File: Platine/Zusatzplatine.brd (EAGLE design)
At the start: 72.1 x 52.1 mm, 29 parts

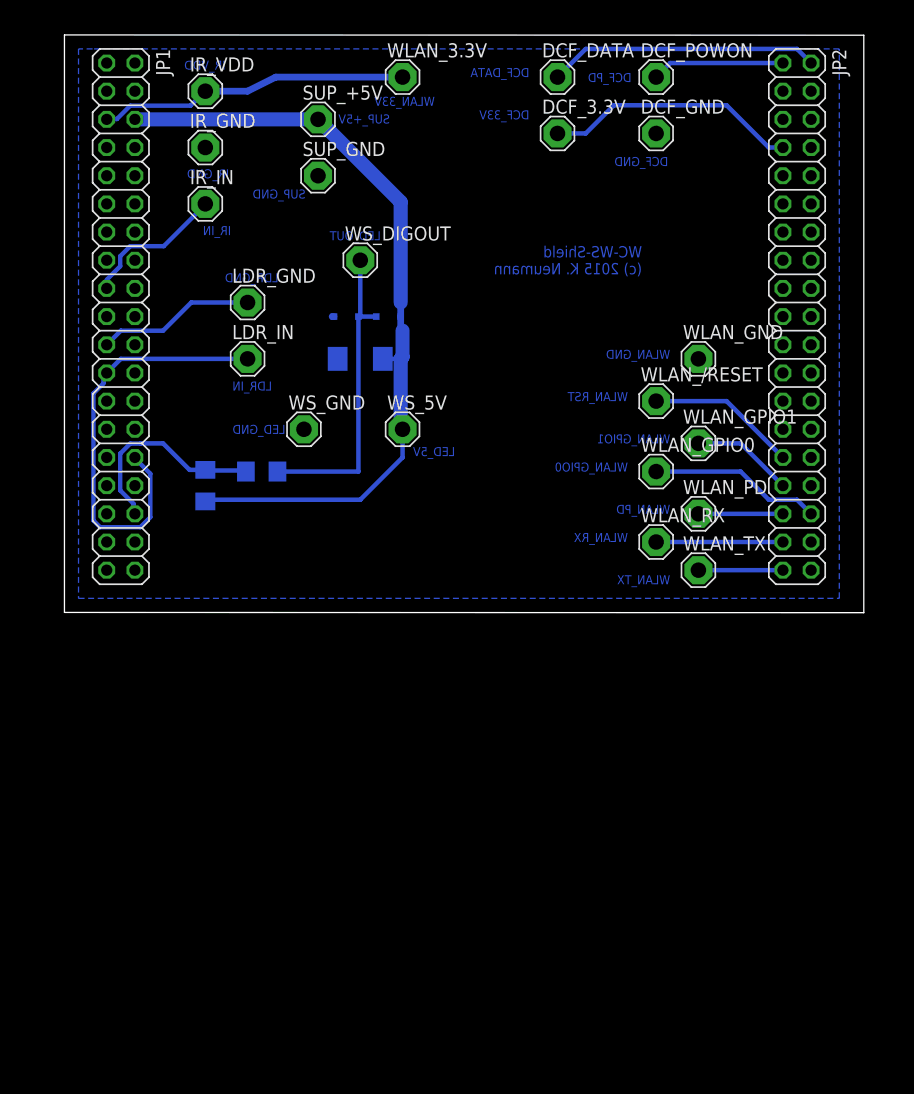
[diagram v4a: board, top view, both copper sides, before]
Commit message: - Platine auf Arduino Connectors umgestellt
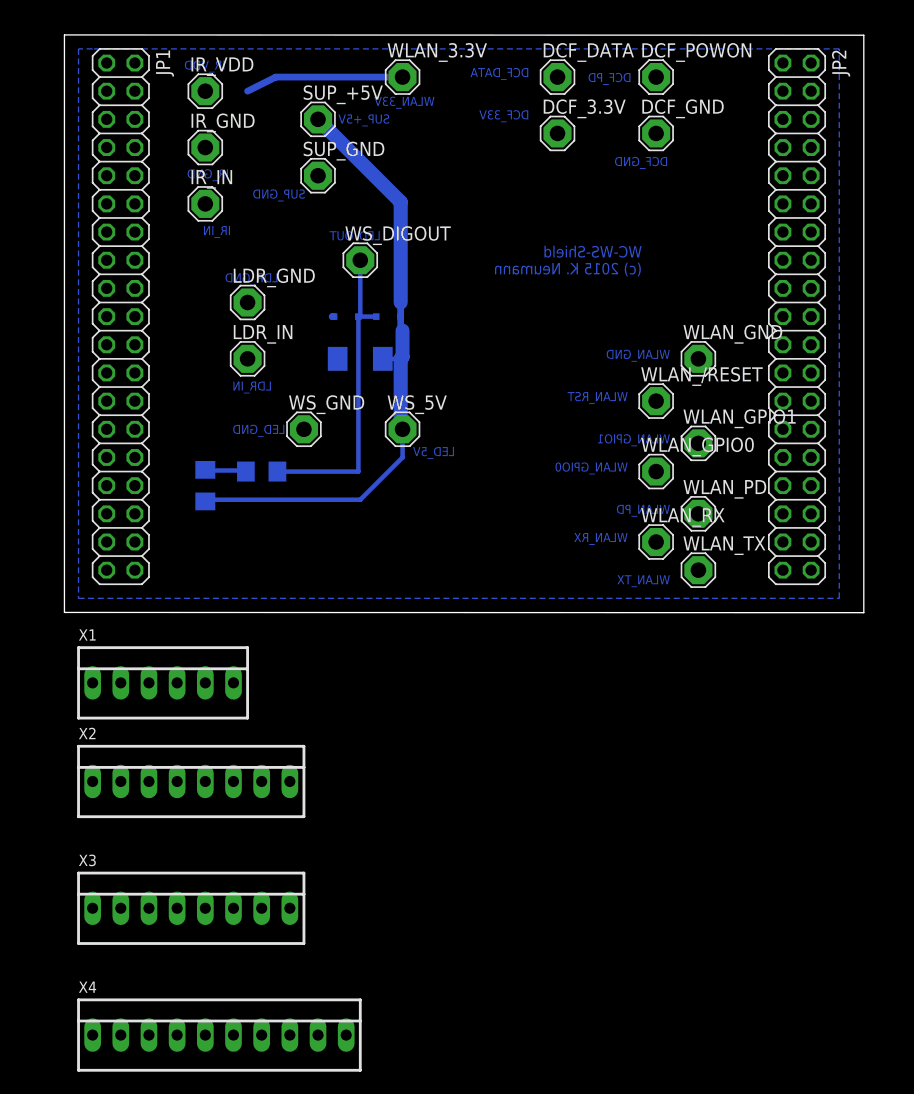
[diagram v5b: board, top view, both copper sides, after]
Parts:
- added X1: (no value), con-molex:22-23-2061
- added X2, X3: 22-23-2081, con-molex:22-23-2081
- added X4: 22-23-2101, con-molex:22-23-2101
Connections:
- removed net N$12: JP2.33, WLAN_PD.MP
- removed net N$13: JP2.35, WLAN_RX.MP
- removed net N$14: JP2.37, WLAN_TX.MP
- removed net N$15: JP2.34, WLAN_GPIO0.MP
- removed net N$18: DCF_3.3V.MP, JP2.7
- removed net N$19: DCF_POWON.MP, JP2.1
- removed net N$20: DCF_DATA.MP, JP2.2
- new net AVDD: X4.3
- new net N$10: DCF_POWON.MP, X4.1
- new net N$5: WLAN_PD.MP, X3.6
- new net N$7: WLAN_/RESET.MP, X3.4
- new net N$9: WLAN_GPIO0.MP, X3.3
- net +3.3V: now also X2.5; no longer JP1.5
- net +5V: now also X2.4; no longer JP1.6
- net GND: now also LDR_GND.MP, X2.2, X2.3; no longer JP1.20, JP1.22, JP1.8, JP2.20, JP2.9, WLAN_GND.MP
- net LED-OUT: now also X1.3; no longer JP1.34
- net N$1: now also WLAN_TX.MP, X3.8; no longer JP2.29, WLAN_/RESET.MP
- net N$11: now also DCF_DATA.MP, X4.2; no longer JP2.31, WLAN_GPIO1.MP
- net N$2: now also X1.6; no longer JP1.17
- net N$3: now also LDR_IN.MP, X1.4, X1.5; no longer JP1.21, LDR_GND.MP
- net N$4: now also WLAN_RX.MP, X3.7; no longer JP1.19
- net N$6: now also WLAN_GPIO1.MP, X3.5; no longer JP1.23, JP1.30, LDR_IN.MP
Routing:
- net N$6: track 38.9 -> 0.00 mm
- net N$20: track 24.4 -> 0.00 mm
- net N$18: track 23.0 -> 0.00 mm
- net +5V: track 71.5 -> 55.0 mm
- net N$15: track 15.5 -> 0.00 mm
- net LED-OUT: track 18.9 -> 3.69 mm
- net N$3: track 14.3 -> 0.00 mm
- net +3.3V: track 28.0 -> 14.3 mm
- net N$1: track 13.5 -> 0.00 mm
- net N$2: track 13.1 -> 0.00 mm
- net N$19: track 12.0 -> 0.00 mm
- net N$13: track 11.4 -> 0.00 mm
- net N$11: track 9.20 -> 0.00 mm
- net N$14: track 7.62 -> 0.00 mm
- net N$12: track 7.62 -> 0.00 mm

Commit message: - Platine überarbeitet
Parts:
- removed JP1, JP2: (no value), pinhead:2X19
- moved X4 88.9 mm to (63.5, 49.5), turned to 270 degrees
- moved X3 62.3 mm to (63.5, 24.1), turned to 270 degrees
- moved X2 45.7 mm to (15.2, 41.9), turned to 90 degrees
- moved IR_IN 20.9 mm to (21.6, 27.9)
- moved WLAN_3.3V 17.7 mm to (27.9, 43.2)
- moved X1 16.7 mm to (15.2, 21.6), turned to 90 degrees
- moved IR_VDD 16.1 mm to (21.6, 43.2)
- moved R2 15.3 mm to (31.8, 21.6), turned to 180 degrees
- moved WLAN_GND 12.7 mm to (48.3, 34.3)
- moved WLAN_PD 12.7 mm to (48.3, 20.3)
- moved WLAN_TX 12.7 mm to (48.3, 15.2)
- moved WS_GND 12.7 mm to (38.1, 27.9)
- moved LDR_IN 11.5 mm to (21.6, 22.9)
- moved WLAN_/RESET 9.67 mm to (48.3, 26.7)
- moved R1 9.25 mm to (30.5, 26.7), turned to 90 degrees
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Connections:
- net AVDD: now also DCF_3.3V.MP
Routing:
- net +5V: track 55.0 -> 23.1 mm
- net LED-OUT: track 3.69 -> 21.4 mm
- net N$11: track 0.00 -> 16.8 mm
- net N$7: track 0.00 -> 15.8 mm
- net AVDD: track 0.00 -> 15.8 mm
- net N$5: track 0.00 -> 15.2 mm
- net N$1: track 0.00 -> 15.2 mm
- net N$9: track 0.00 -> 12.5 mm
- net N$6: track 0.00 -> 12.0 mm
- net N$4: track 0.00 -> 11.4 mm
- net N$3: track 0.00 -> 8.89 mm
- net N$10: track 0.00 -> 6.88 mm
- net N$2: track 0.00 -> 6.35 mm
- net N$8: track 28.1 -> 21.8 mm
- net +3.3V: track 14.3 -> 12.7 mm
- added copper zone on layer 1, net +5V
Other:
- board size 72.1 x 52.1 mm -> 55.6 x 49.5 mm
- board text added: "IR_+3.3V"
- board text removed: "IR_VDD"

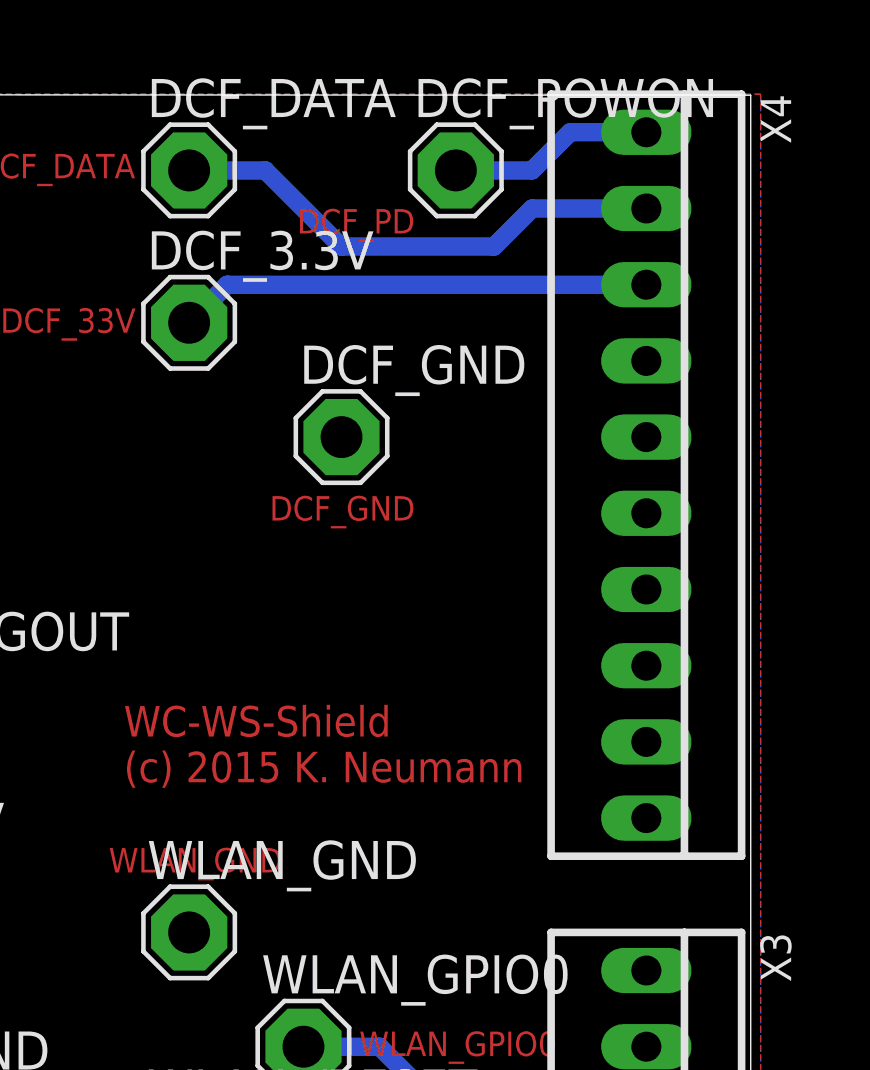
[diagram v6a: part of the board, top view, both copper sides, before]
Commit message: Corrected layout of top right pin row for arduino interfacing
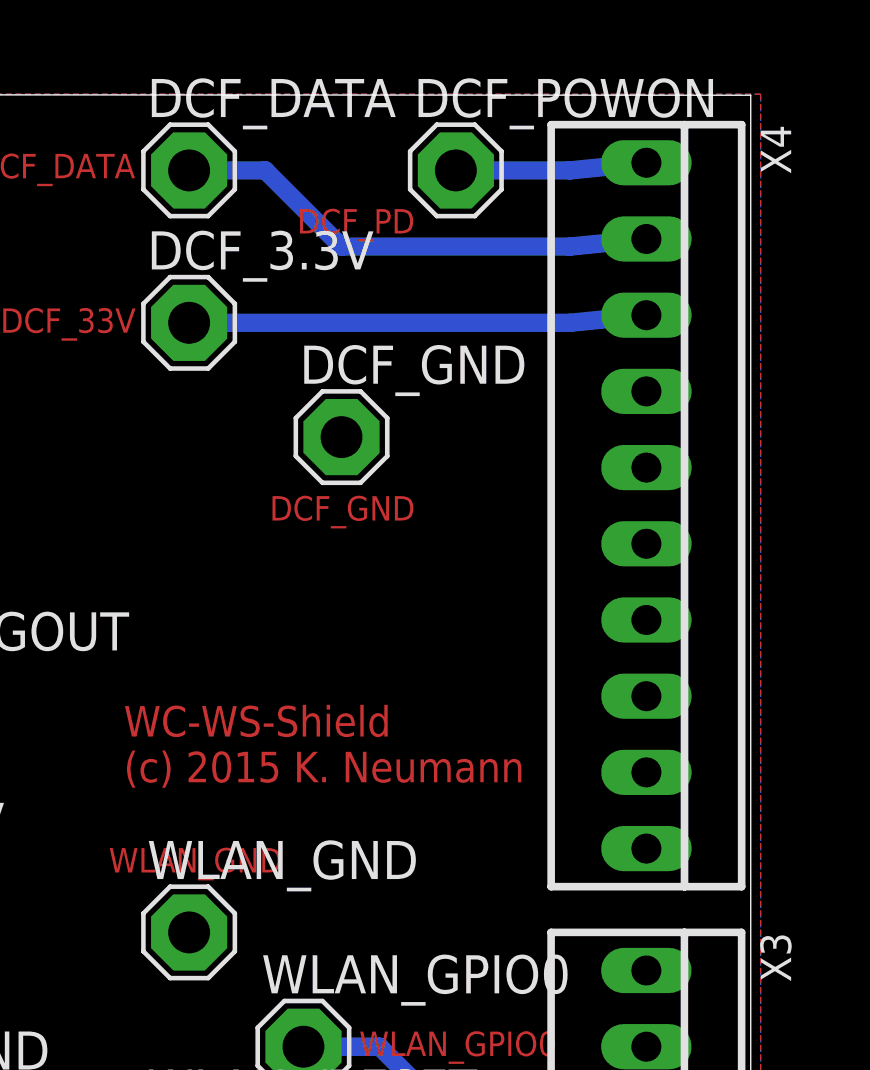
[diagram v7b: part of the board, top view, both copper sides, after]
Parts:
- moved X4 1.02 mm to (63.5, 48.5)
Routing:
- net N$11: track 16.8 -> 16.3 mm
- net N$10: track 6.88 -> 6.36 mm
- net AVDD: track 15.8 -> 15.3 mm
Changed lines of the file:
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@@
 <?xml version="1.0" encoding="utf-8"?>
 <!DOCTYPE eagle SYSTEM "eagle.dtd">
-<eagle version="7.4.0">
+<eagle version="7.2.0">
 <drawing>
 <settings>
@@
 <layer number="48" name="Document" color="7" fill="1" visible="yes" active="yes"/>
 <layer number="49" name="Reference" color="7" fill="1" visible="yes" active="yes"/>
+<layer number="50" name="dxf" color="7" fill="1" visible="no" active="yes"/>
 <layer number="51" name="tDocu" color="7" fill="1" visible="yes" active="yes"/>
 <layer number="52" name="bDocu" color="7" fill="1" visible="yes" active="yes"/>
+<layer number="53" name="tGND_GNDA" color="7" fill="9" visible="no" active="no"/>
+<layer number="54" name="bGND_GNDA" color="1" fill="9" visible="no" active="no"/>
+<layer number="56" name="wert" color="7" fill="1" visible="no" active="yes"/>
+<layer number="57" name="tCAD" color="7" fill="1" visible="no" active="no"/>
 <layer number="90" name="Modules" color="5" fill="1" visible="no" active="no"/>
 <layer number="91" name="Nets" color="2" fill="1" visible="no" active="no"/>
@@
 <layer number="98" name="Guide" color="6" fill="1" visible="no" active="no"/>
 <layer number="99" name="SpiceOrder" color="5" fill="1" visible="no" active="no"/>
+<layer number="100" name="Muster" color="7" fill="1" visible="no" active="no"/>
+<layer number="101" name="Patch_Top" color="12" fill="4" visible="no" active="yes"/>
+<layer number="102" name="Vscore" color="7" fill="1" visible="no" active="yes"/>
+<layer number="103" name="fp3" color="7" fill="1" visible="no" active="yes"/>
+<layer number="104" name="Name" color="7" fill="1" visible="no" active="yes"/>
+<layer number="105" name="Beschreib" color="9" fill="1" visible="no" active="yes"/>
+<layer number="106" name="BGA-Top" color="4" fill="1" visible="no" active="yes"/>
+<layer number="107" name="BD-Top" color="5" fill="1" visible="no" active="yes"/>
+<layer number="108" name="fp8" color="7" fill="1" visible="no" active="yes"/>
+<layer number="109" name="fp9" color="7" fill="1" visible="no" active="yes"/>
+<layer number="110" name="fp0" color="7" fill="1" visible="no" active="yes"/>
+<layer number="111" name="LPC17xx" color="7" fill="1" visible="no" active="yes"/>
+<layer number="112" name="tSilk" color="7" fill="1" visible="no" active="yes"/>
+<layer number="113" name="ReferenceLS" color="7" fill="1" visible="no" active="no"/>
+<layer number="116" name="Patch_BOT" color="9" fill="4" visible="no" active="yes"/>
+<layer number="118" name="Rect_Pads" color="7" fill="1" visible="no" active="no"/>
+<layer number="121" name="_tsilk" color="7" fill="1" visible="no" active="yes"/>
+<layer number="122" name="_bsilk" color="7" fill="1" visible="no" active="yes"/>
+<layer number="123" name="tTestmark" color="7" fill="1" visible="no" active="yes"/>
+<layer number="124" name="bTestmark" color="7" fill="1" visible="no" active="yes"/>
+<layer number="125" name="_tNames" color="7" fill="1" visible="no" active="yes"/>
+<layer number="126" name="_bNames" color="7" fill="1" visible="no" active="yes"/>
+<layer number="127" name="_tValues" color="7" fill="1" visible="no" active="yes"/>
+<layer number="128" name="_bValues" color="7" fill="1" visible="no" active="yes"/>
+<layer number="131" name="tAdjust" color="7" fill="1" visible="no" active="yes"/>
+<layer number="132" name="bAdjust" color="7" fill="1" visible="no" active="yes"/>
+<layer number="144" name="Drill_legend" color="7" fill="1" visible="no" active="yes"/>
+<layer number="150" name="Notes" color="7" fill="1" visible="no" active="yes"/>
+<layer number="151" name="HeatSink" color="7" fill="1" visible="no" active="yes"/>
+<layer number="152" name="_bDocu" color="7" fill="1" visible="no" active="yes"/>
+<layer number="153" name="FabDoc1" color="6" fill="1" visible="no" active="no"/>
+<layer number="154" name="FabDoc2" color="2" fill="1" visible="no" active="no"/>
+<layer number="155" name="FabDoc3" color="7" fill="15" visible="no" active="no"/>
+<layer number="199" name="Contour" color="7" fill="1" visible="no" active="yes"/>
+<layer number="200" name="200bmp" color="1" fill="10" visible="no" active="yes"/>
+<layer number="201" name="201bmp" color="2" fill="1" visible="no" active="no"/>
+<layer number="202" name="202bmp" color="3" fill="1" visible="no" active="no"/>
+<layer number="203" name="203bmp" color="4" fill="10" visible="no" active="yes"/>
+<layer number="204" name="204bmp" color="5" fill="10" visible="no" active="yes"/>
+<layer number="205" name="205bmp" color="6" fill="10" visible="no" active="yes"/>
+<layer number="206" name="206bmp" color="7" fill="10" visible="no" active="yes"/>
+<layer number="207" name="207bmp" color="8" fill="10" visible="no" active="yes"/>
+<layer number="208" name="208bmp" color="9" fill="10" visible="no" active="yes"/>
+<layer number="209" name="209bmp" color="7" fill="1" visible="no" active="yes"/>
+<layer number="210" name="210bmp" color="7" fill="1" visible="no" active="yes"/>
+<layer number="211" name="211bmp" color="7" fill="1" visible="no" active="yes"/>
+<layer number="212" name="212bmp" color="7" fill="1" visible="no" active="yes"/>
+<layer number="213" name="213bmp" color="7" fill="1" visible="no" active="yes"/>
+<layer number="214" name="214bmp" color="7" fill="1" visible="no" active="yes"/>
+<layer number="215" name="215bmp" color="7" fill="1" visible="no" active="yes"/>
+<layer number="216" name="216bmp" color="7" fill="1" visible="no" active="yes"/>
+<layer number="217" name="217bmp" color="18" fill="1" visible="no" active="no"/>
+<layer number="218" name="218bmp" color="19" fill="1" visible="no" active="no"/>
+<layer number="219" name="219bmp" color="20" fill="1" visible="no" active="no"/>
+<layer number="220" name="220bmp" color="21" fill="1" visible="no" active="no"/>
+<layer number="221" name="221bmp" color="22" fill="1" visible="no" active="no"/>
+<layer number="222" name="222bmp" color="23" fill="1" visible="no" active="no"/>
+<layer number="223" name="223bmp" color="24" fill="1" visible="no" active="no"/>
+<layer number="224" name="224bmp" color="25" fill="1" visible="no" active="no"/>
+<layer number="231" name="Eagle3D_PG1" color="7" fill="1" visible="no" active="no"/>
+<layer number="232" name="Eagle3D_PG2" color="7" fill="1" visible="no" active="no"/>
+<layer number="233" name="Eagle3D_PG3" color="7" fill="1" visible="no" active="no"/>
+<layer number="248" name="Housing" color="7" fill="1" visible="no" active="yes"/>
+<layer number="249" name="Edge" color="7" fill="1" visible="no" active="yes"/>
+<layer number="250" name="Descript" color="7" fill="1" visible="no" active="no"/>
+<layer number="251" name="SMDround" color="7" fill="1" visible="no" active="no"/>
+<layer number="254" name="cooling" color="7" fill="1" visible="no" active="yes"/>
 </layers>
 <board>
@@
 <attribute name="MF" value="MOLEX" x="63.5" y="24.13" size="1.778" layer="27" rot="R270" display="off"/>
 </element>
-<element name="X4" library="con-molex" package="22-23-2101" value="22-23-2101" x="63.5" y="49.53" rot="R270">
-<attribute name="OC_FARNELL" value="1756828" x="63.5" y="49.53" size="1.778" layer="27" rot="R270" display="off"/>
-<attribute name="OC_NEWARK" value="94C0765" x="63.5" y="49.53" size="1.778" layer="27" rot="R270" display="off"/>
-<attribute name="MPN" value="22-23-2101" x="63.5" y="49.53" size="1.778" layer="27" rot="R270" display="off"/>
-<attribute name="MF" value="MOLEX" x="63.5" y="49.53" size="1.778" layer="27" rot="R270" display="off"/>
+<element name="X4" library="con-molex" package="22-23-2101" value="22-23-2101" x="63.502121875" y="48.51419375" rot="R270">
+<attribute name="OC_FARNELL" value="1756828" x="63.502121875" y="48.51419375" size="1.778" layer="27" rot="R270" display="off"/>
+<attribute name="OC_NEWARK" value="94C0765" x="63.502121875" y="48.51419375" size="1.778" layer="27" rot="R270" display="off"/>
+<attribute name="MPN" value="22-23-2101" x="63.502121875" y="48.51419375" size="1.778" layer="27" rot="R270" display="off"/>
+<attribute name="MF" value="MOLEX" x="63.502121875" y="48.51419375" size="1.778" layer="27" rot="R270" display="off"/>
 </element>
 </elements>
@@
 <contactref element="X4" pad="3"/>
 <contactref element="DCF_3.3V" pad="MP"/>
-<wire x1="48.26" y1="54.61" x2="49.53" y2="55.88" width="0.6096" layer="16"/>
-<wire x1="49.53" y1="55.88" x2="63.5" y2="55.88" width="0.6096" layer="16"/>
+<wire x1="48.26" y1="54.61" x2="60.96" y2="54.61" width="0.6096" layer="16"/>
+<wire x1="60.96" y1="54.61" x2="63.502121875" y2="54.86419375" width="0.6096" layer="16"/>
 </signal>
 <signal name="N$1">
@@
 <contactref element="DCF_POWON" pad="MP"/>
 <contactref element="X4" pad="1"/>
-<wire x1="63.5" y1="60.96" x2="60.96" y2="60.96" width="0.6096" layer="16"/>
-<wire x1="60.96" y1="60.96" x2="59.69" y2="59.69" width="0.6096" layer="16"/>
-<wire x1="59.69" y1="59.69" x2="57.15" y2="59.69" width="0.6096" layer="16"/>
+<wire x1="63.502121875" y1="59.94419375" x2="60.96" y2="59.69" width="0.6096" layer="16"/>
+<wire x1="60.96" y1="59.69" x2="57.15" y2="59.69" width="0.6096" layer="16"/>
 </signal>
 <signal name="N$11">
 <contactref element="X4" pad="2"/>
 <contactref element="DCF_DATA" pad="MP"/>
-<wire x1="63.5" y1="58.42" x2="59.69" y2="58.42" width="0.6096" layer="16"/>
-<wire x1="59.69" y1="58.42" x2="58.42" y2="57.15" width="0.6096" layer="16"/>
-<wire x1="58.42" y1="57.15" x2="53.34" y2="57.15" width="0.6096" layer="16"/>
+<wire x1="63.502121875" y1="57.40419375" x2="60.96" y2="57.15" width="0.6096" layer="16"/>
+<wire x1="60.96" y1="57.15" x2="53.34" y2="57.15" width="0.6096" layer="16"/>
 <wire x1="53.34" y1="57.15" x2="50.8" y2="59.69" width="0.6096" layer="16"/>
 <wire x1="50.8" y1="59.69" x2="48.26" y2="59.69" width="0.6096" layer="16"/>
